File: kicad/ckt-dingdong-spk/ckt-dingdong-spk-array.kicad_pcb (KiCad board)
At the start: 2 copper layers, 96.5 x 96.5 mm, 224 parts, among them J1 Conn_01x02_MountingPin

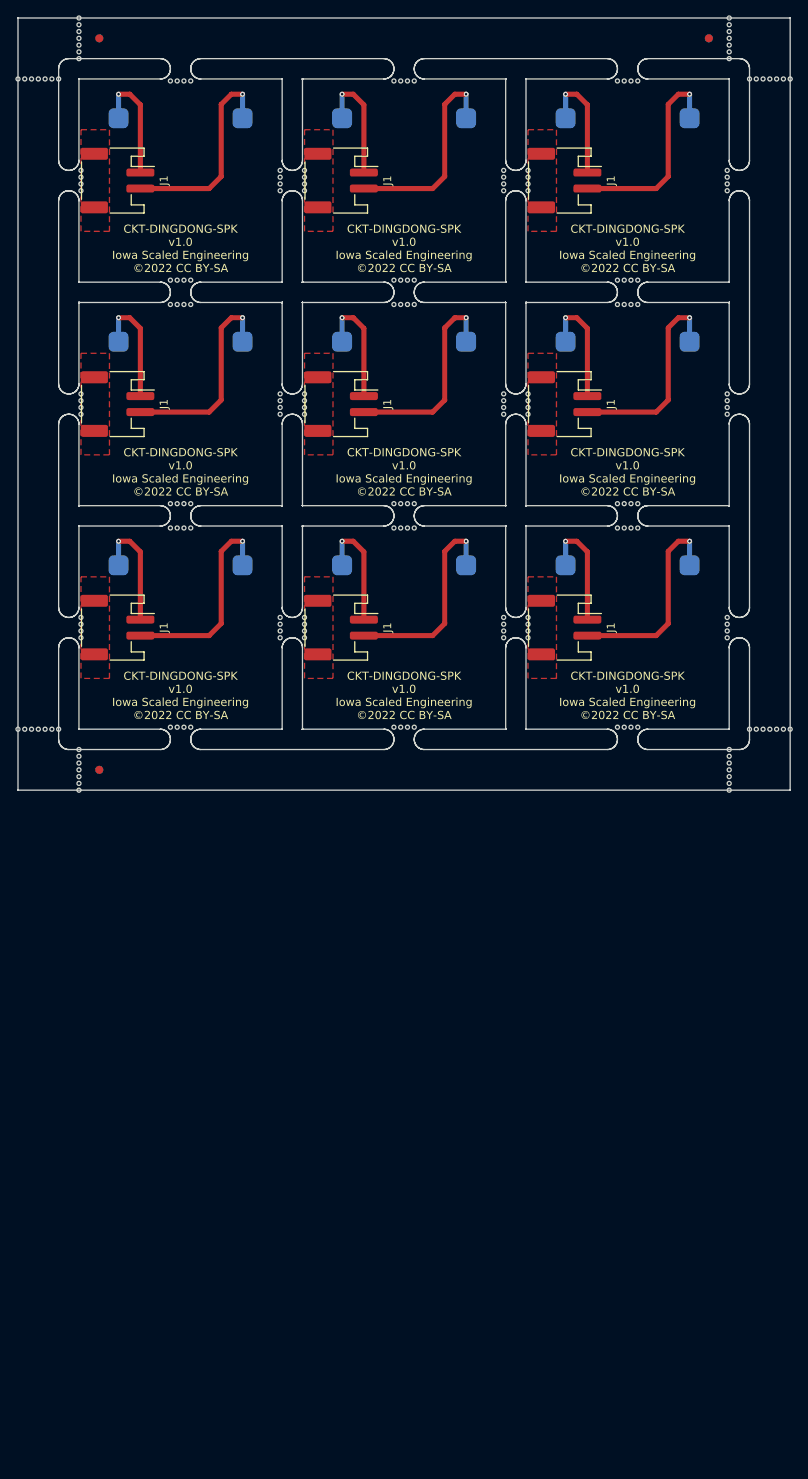
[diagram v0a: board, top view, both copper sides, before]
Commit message: Added array board
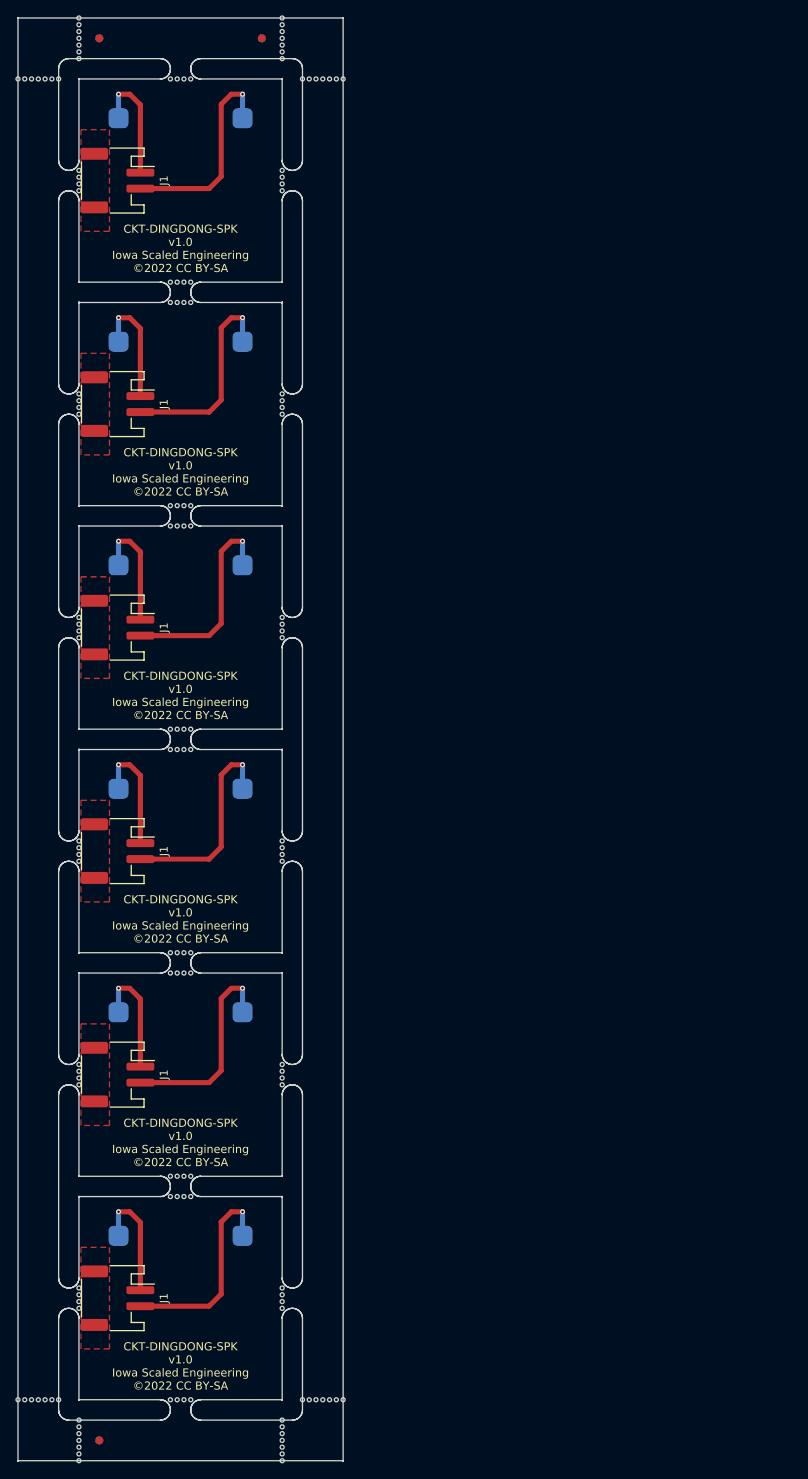
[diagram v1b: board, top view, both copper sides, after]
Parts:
- removed the J1 at (83.3, 91.2)
- removed the J1 at (55.4, 91.2)
- removed the J1 at (27.4, 91.2)
- removed the REF** at (19.2, 103.9)
- removed the REF** at (75.7, 63.7)
- removed the REF** at (36.6, 50.8)
- removed the REF** at (78.8, 64.5)
- removed the REF** at (92.5, 75.7)
- removed the REF** at (34.9, 103.7)
- removed the REF** at (34.9, 75.7)
- removed the REF** at (50.8, 64.5)
- removed the REF** at (78.8, 34.9)
- removed the REF** at (75.7, 34.0)
- removed the REF** at (47.8, 62.8)
- removed the REF** at (63.7, 75.7)
- removed the REF** at (78.8, 91.6)
- removed the REF** at (62.8, 47.8)
- removed the REF** at (90.8, 50.8)
- removed the REF** at (64.5, 50.8)
- removed the REF** at (22.9, 90.8)
- removed the REF** at (75.7, 36.6)
- removed the REF** at (103.9, 107.3)
- removed the REF** at (75.7, 34.9)
- removed the REF** at (106.4, 22.6)
- removed the REF** at (90.8, 103.7)
- removed the REF** at (103.7, 89.9)
- removed the REF** at (34.9, 78.8)
- removed the REF** at (50.8, 63.7)
- removed the REF** at (63.7, 78.8)
- removed the REF** at (34.0, 75.7)
- removed the REF** at (63.7, 50.8)
- removed the REF** at (47.8, 62.0)
- removed the REF** at (91.6, 50.8)
- removed the REF** at (17.5, 103.9)
- removed the REF** at (47.8, 89.9)
- removed the REF** at (103.9, 109.0)
- removed the REF** at (103.7, 34.9)
- removed the REF** at (50.8, 35.7)
- removed the REF** at (22.6, 107.3)
- removed the REF** at (62.8, 50.8)
- removed the REF** at (103.9, 110.7)
- removed the REF** at (50.8, 62.0)
- removed the REF** at (63.7, 103.7)
- removed the REF** at (92.5, 78.8)
- removed the REF** at (78.8, 62.0)
- removed the REF** at (75.7, 90.8)
- removed the REF** at (50.8, 92.5)
- removed the REF** at (50.8, 90.8)
- removed the REF** at (22.9, 35.7)
- removed the REF** at (62.0, 47.8)
- removed the REF** at (103.7, 36.6)
- removed the REF** at (103.9, 19.2)
- removed the REF** at (22.9, 62.8)
- removed the REF** at (108.1, 103.9)
- removed the REF** at (78.8, 35.7)
- removed the REF** at (106.4, 103.9)
- removed the REF** at (91.6, 22.9)
- removed the REF** at (78.8, 62.8)
- removed the REF** at (22.6, 111.5)
- removed the REF** at (103.9, 20.1)
- removed the REF** at (34.0, 78.8)
- removed the REF** at (89.9, 47.8)
- removed the REF** at (18.4, 103.9)
- removed the REF** at (91.6, 103.7)
- removed the REF** at (36.6, 47.8)
- removed the REF** at (36.6, 103.7)
- removed the REF** at (47.8, 91.6)
- removed the REF** at (64.5, 78.8)
- removed the REF** at (75.7, 35.7)
- removed the REF** at (50.8, 89.9)
- removed the REF** at (78.8, 92.5)
- removed the REF** at (34.9, 50.8)
- removed the REF** at (34.0, 47.8)
- removed the REF** at (110.7, 103.9)
- removed the REF** at (15.0, 103.9)
- removed the REF** at (90.8, 75.7)
- removed the REF** at (22.6, 110.7)
- removed the REF** at (101.4, 17.5) (x2)
- removed the REF** at (62.0, 22.9)
- removed the REF** at (108.1, 22.6)
- removed the REF** at (111.5, 22.6)
- removed the REF** at (103.9, 108.1)
- removed the REF** at (50.8, 34.9)
- removed the REF** at (35.7, 50.8)
- removed the REF** at (89.9, 103.7)
- removed the REF** at (89.9, 22.9)
- removed the REF** at (34.0, 103.7)
- removed the REF** at (63.7, 47.8)
- removed the REF** at (22.9, 64.5)
- removed the REF** at (47.8, 92.5)
- removed the REF** at (109.0, 22.6)
- removed the REF** at (62.8, 75.7)
- removed the REF** at (103.7, 34.0)
- removed the REF** at (103.7, 35.7)
- removed the REF** at (75.7, 62.0)
- removed the REF** at (22.6, 109.8)
- removed the REF** at (103.7, 62.0)
- removed the REF** at (15.8, 103.9)
- removed the REF** at (92.5, 22.9)
- removed the REF** at (47.8, 64.5)
- removed the REF** at (47.8, 90.8)
- removed the REF** at (22.9, 92.5)
- removed the REF** at (35.7, 47.8)
- removed the REF** at (78.8, 34.0)
- removed the REF** at (62.8, 78.8)
- removed the REF** at (75.7, 91.6)
- removed the REF** at (22.6, 109.0)
- removed the REF** at (78.8, 90.8)
- removed the REF** at (62.0, 50.8)
- removed the REF** at (35.7, 75.7)
- removed the REF** at (89.9, 50.8)
- removed the REF** at (25.2, 109.0) (x2)
- removed the REF** at (25.2, 17.5) (x2)
- removed the REF** at (75.7, 62.8)
- removed the REF** at (22.9, 62.0)
- removed the REF** at (78.8, 89.9)
- removed the REF** at (103.9, 16.7)
- removed the REF** at (35.7, 103.7)
- removed the REF** at (47.8, 34.0)
- removed the REF** at (63.7, 22.9)
- removed the REF** at (35.7, 22.9)
- removed the REF** at (62.8, 22.9)
- removed the REF** at (62.0, 103.7)
- removed the REF** at (22.9, 91.6)
- removed the REF** at (62.8, 103.7)
- removed the REF** at (109.8, 103.9)
- removed the REF** at (91.6, 47.8)
- removed the REF** at (103.7, 91.6)
- removed the REF** at (92.5, 47.8)
- removed the REF** at (103.9, 15.0)
- removed the REF** at (107.3, 22.6)
- removed the REF** at (34.9, 47.8)
- removed the REF** at (111.5, 103.9)
- removed the REF** at (64.5, 103.7)
- removed the REF** at (22.6, 108.1)
- removed the REF** at (78.8, 36.6)
- removed the REF** at (16.7, 103.9)
- removed the REF** at (92.5, 50.8)
- removed the REF** at (47.8, 36.6)
- removed the REF** at (22.9, 34.9)
- removed the REF** at (91.6, 75.7)
- removed the REF** at (103.9, 15.8)
- removed the REF** at (109.0, 103.9)
- removed the REF** at (47.8, 35.7)
- removed the REF** at (75.7, 92.5)
- removed the REF** at (36.6, 78.8)
- removed the REF** at (64.5, 47.8)
- removed the REF** at (75.7, 89.9)
- removed the REF** at (103.7, 90.8)
- removed the REF** at (22.6, 106.4)
- removed the REF** at (103.9, 111.5)
- removed the REF** at (90.8, 78.8)
- removed the REF** at (91.6, 78.8)
- removed the REF** at (110.7, 22.6)
- removed the REF** at (64.5, 22.9)
- removed the REF** at (22.9, 36.6)
- removed the REF** at (22.9, 63.7)
- removed the REF** at (36.6, 75.7)
- removed the REF** at (50.8, 62.8)
- removed the REF** at (75.7, 64.5)
- removed the REF** at (22.9, 34.0)
- removed the REF** at (62.0, 75.7)
- removed the REF** at (34.0, 22.9)
- removed the REF** at (20.1, 103.9)
- removed the REF** at (92.5, 103.7)
- removed the REF** at (50.8, 34.0)
- removed the REF** at (103.9, 18.4)
- removed the REF** at (103.7, 64.5)
- removed the REF** at (109.8, 22.6)
- removed the REF** at (103.7, 92.5)
- removed the REF** at (47.8, 63.7)
- removed the REF** at (36.6, 22.9)
- removed the REF** at (50.8, 36.6)
- removed the REF** at (22.9, 89.9)
- removed the REF** at (103.9, 106.4)
- removed the REF** at (90.8, 47.8)
- removed the REF** at (89.9, 78.8)
- removed the REF** at (90.8, 22.9)
- removed the REF** at (35.7, 78.8)
- removed the REF** at (103.7, 62.8)
- removed the REF** at (50.8, 91.6)
- removed the REF** at (103.9, 17.5)
- removed the REF** at (103.7, 63.7)
- removed the REF** at (107.3, 103.9)
- removed the REF** at (89.9, 75.7)
- removed the REF** at (103.9, 109.8)
- removed the REF** at (62.0, 78.8)
- removed the REF** at (34.9, 22.9)
- removed the REF** at (64.5, 75.7)
- removed the REF** at (78.8, 63.7)
- removed the REF** at (47.8, 34.9)
- removed the REF** at (34.0, 50.8)
- removed the SPK1 at (35.3, 88.7)
- removed the SPK1 at (63.3, 88.7)
- removed the SPK1 at (91.2, 88.7)
- added REF**: NPTH, NPTH, F.Cu at (53.9, 187.7)
- added REF**: NPTH, NPTH, F.Cu at (34.9, 134.4)
- added REF**: Fiducial, Fiducial, F.Cu at (45.5, 17.5)
- added REF**: NPTH, NPTH, F.Cu at (34.9, 76.0)
- added REF**: NPTH, NPTH, F.Cu at (34.9, 48.0)
- added REF**: NPTH, NPTH, F.Cu at (36.6, 48.0)
- added REF**: NPTH, NPTH, F.Cu at (52.3, 22.6)
- added REF**: NPTH, NPTH, F.Cu at (22.6, 194.5)
- added REF**: NPTH, NPTH, F.Cu at (22.6, 118.7)
- added REF**: NPTH, NPTH, F.Cu at (35.7, 187.7)
- added REF**: NPTH, NPTH, F.Cu at (48.0, 191.1)
- added REF**: NPTH, NPTH, F.Cu at (22.6, 147.5)
- added REF**: NPTH, NPTH, F.Cu at (55.6, 187.7)
- added REF**: NPTH, NPTH, F.Cu at (48.0, 194.5)
- added REF**: NPTH, NPTH, F.Cu at (36.6, 162.3)
- added REF**: NPTH, NPTH, F.Cu at (36.6, 22.6)
- added REF**: NPTH, NPTH, F.Cu at (34.9, 106.4)
- added REF**: NPTH, NPTH, F.Cu at (48.0, 120.4)
- added REF**: NPTH, NPTH, F.Cu at (48.0, 18.4)
- added REF**: NPTH, NPTH, F.Cu at (34.0, 134.4)
- added REF**: NPTH, NPTH, F.Cu at (22.6, 36.6)
- added REF**: NPTH, NPTH, F.Cu at (22.6, 92.5)
- added REF**: NPTH, NPTH, F.Cu at (17.5, 187.7)
- added REF**: NPTH, NPTH, F.Cu at (48.0, 192.0)
- added REF**: NPTH, NPTH, F.Cu at (22.6, 34.0)
- added REF**: NPTH, NPTH, F.Cu at (53.9, 22.6)
- added REF**: NPTH, NPTH, F.Cu at (19.2, 187.7)
- added REF**: NPTH, NPTH, F.Cu at (34.0, 159.8)
- added REF**: NPTH, NPTH, F.Cu at (36.6, 50.6)
- added REF**: NPTH, NPTH, F.Cu at (22.6, 174.6)
- added REF**: NPTH, NPTH, F.Cu at (48.0, 90.8)
- added REF**: NPTH, NPTH, F.Cu at (22.6, 191.1)
- added REF**: NPTH, NPTH, F.Cu at (34.9, 159.8)
- added REF**: NPTH, NPTH, F.Cu at (15.0, 187.7)
- added REF**: NPTH, NPTH, F.Cu at (22.6, 146.7)
- added REF**: NPTH, NPTH, F.Cu at (34.9, 187.7)
- added REF**: NPTH, NPTH, F.Cu at (22.6, 62.0)
- added REF**: NPTH, NPTH, F.Cu at (34.9, 131.8)
- added REF**: NPTH, NPTH, F.Cu at (48.0, 92.5)
- added REF**: NPTH, NPTH, F.Cu at (22.6, 34.9)
- added REF**: NPTH, NPTH, F.Cu at (36.6, 78.5)
- added REF**: NPTH, NPTH, F.Cu at (35.7, 22.6)
- added REF**: NPTH, NPTH, F.Cu at (22.6, 119.6)
- added REF**: NPTH, NPTH, F.Cu at (22.6, 175.4)
- added REF**: NPTH, NPTH, F.Cu at (48.0, 15.0)
- added REF**: NPTH, NPTH, F.Cu at (35.7, 50.6)
- added REF**: NPTH, NPTH, F.Cu at (50.6, 22.6)
- added REF**: NPTH, NPTH, F.Cu at (48.0, 190.3)
- added REF**: NPTH, NPTH, F.Cu at (35.7, 78.5)
- added REF**: NPTH, NPTH, F.Cu at (34.0, 106.4)
- added REF**: NPTH, NPTH, F.Cu at (51.4, 187.7)
- added REF**: NPTH, NPTH, F.Cu at (48.0, 176.3)
- added REF**: NPTH, NPTH, F.Cu at (22.6, 176.3)
- added REF**: NPTH, NPTH, F.Cu at (34.9, 50.6)
- added REF**: NPTH, NPTH, F.Cu at (34.0, 50.6)
- added REF**: NPTH, NPTH, F.Cu at (22.6, 35.7)
- added REF**: NPTH, NPTH, F.Cu at (36.6, 159.8)
- added REF**: Fiducial, Fiducial, B.Cu at (25.2, 192.8)
- added REF**: Fiducial, Fiducial, B.Cu at (45.5, 17.5)
- added REF**: Fiducial, Fiducial, B.Cu at (25.2, 17.5)
- added REF**: NPTH, NPTH, F.Cu at (36.6, 106.4)
- added REF**: NPTH, NPTH, F.Cu at (34.9, 78.5)
- added REF**: NPTH, NPTH, F.Cu at (35.7, 131.8)
- added REF**: NPTH, NPTH, F.Cu at (48.0, 35.7)
- added REF**: NPTH, NPTH, F.Cu at (35.7, 48.0)
- added REF**: NPTH, NPTH, F.Cu at (35.7, 162.3)
- added REF**: NPTH, NPTH, F.Cu at (48.0, 20.1)
- added REF**: NPTH, NPTH, F.Cu at (48.0, 147.5)
- added REF**: NPTH, NPTH, F.Cu at (22.6, 120.4)
- added REF**: NPTH, NPTH, F.Cu at (34.0, 78.5)
- added REF**: NPTH, NPTH, F.Cu at (22.6, 195.3)
- added REF**: NPTH, NPTH, F.Cu at (52.3, 187.7)
- added REF**: NPTH, NPTH, F.Cu at (36.6, 76.0)
- added REF**: NPTH, NPTH, F.Cu at (22.6, 193.6)
- added REF**: NPTH, NPTH, F.Cu at (15.8, 187.7)
- added REF**: NPTH, NPTH, F.Cu at (48.0, 17.5)
- added REF**: NPTH, NPTH, F.Cu at (48.0, 118.7)
- added REF**: NPTH, NPTH, F.Cu at (54.8, 187.7)
- added REF**: NPTH, NPTH, F.Cu at (16.7, 187.7)
- added REF**: NPTH, NPTH, F.Cu at (48.0, 62.8)
- added REF**: NPTH, NPTH, F.Cu at (48.0, 64.5)
- added REF**: NPTH, NPTH, F.Cu at (20.1, 187.7)
- added REF**: NPTH, NPTH, F.Cu at (53.1, 22.6)
- added REF**: NPTH, NPTH, F.Cu at (22.6, 64.5)
- added REF**: NPTH, NPTH, F.Cu at (48.0, 36.6)
- added REF**: NPTH, NPTH, F.Cu at (36.6, 131.8)
- added REF**: NPTH, NPTH, F.Cu at (48.0, 173.8)
- added REF**: NPTH, NPTH, F.Cu at (36.6, 187.7)
- added REF**: NPTH, NPTH, F.Cu at (35.7, 106.4)
- added REF**: NPTH, NPTH, F.Cu at (22.6, 63.7)
- added REF**: NPTH, NPTH, F.Cu at (36.6, 103.9)
- added REF**: NPTH, NPTH, F.Cu at (35.7, 159.8)
- added REF**: Fiducial, Fiducial, F.Cu at (25.2, 17.5)
- added REF**: NPTH, NPTH, F.Cu at (22.6, 192.0)
- added REF**: NPTH, NPTH, F.Cu at (48.0, 148.3)
- added REF**: NPTH, NPTH, F.Cu at (22.6, 91.6)
- added REF**: NPTH, NPTH, F.Cu at (22.6, 62.8)
- added REF**: NPTH, NPTH, F.Cu at (54.8, 22.6)
- added REF**: NPTH, NPTH, F.Cu at (48.0, 62.0)
- added REF**: NPTH, NPTH, F.Cu at (34.0, 22.6)
- added REF**: NPTH, NPTH, F.Cu at (48.0, 16.7)
- added REF**: NPTH, NPTH, F.Cu at (34.0, 162.3)
- added REF**: NPTH, NPTH, F.Cu at (48.0, 34.0)
- added REF**: NPTH, NPTH, F.Cu at (34.0, 103.9)
- added REF**: NPTH, NPTH, F.Cu at (36.6, 134.4)
- added REF**: NPTH, NPTH, F.Cu at (48.0, 34.9)
- added REF**: NPTH, NPTH, F.Cu at (48.0, 89.9)
- added REF**: NPTH, NPTH, F.Cu at (35.7, 134.4)
- added REF**: NPTH, NPTH, F.Cu at (48.0, 19.2)
- added REF**: NPTH, NPTH, F.Cu at (34.0, 76.0)
- added REF**: NPTH, NPTH, F.Cu at (18.4, 187.7)
- added REF**: NPTH, NPTH, F.Cu at (34.0, 187.7)
- added REF**: NPTH, NPTH, F.Cu at (22.6, 145.8)
- added REF**: NPTH, NPTH, F.Cu at (50.6, 187.7)
- added REF**: NPTH, NPTH, F.Cu at (35.7, 103.9)
- added REF**: NPTH, NPTH, F.Cu at (48.0, 193.6)
- added REF**: NPTH, NPTH, F.Cu at (34.0, 48.0)
- added REF**: NPTH, NPTH, F.Cu at (48.0, 174.6)
- added REF**: NPTH, NPTH, F.Cu at (34.0, 131.8)
- added REF**: NPTH, NPTH, F.Cu at (35.7, 76.0)
- added REF**: NPTH, NPTH, F.Cu at (48.0, 119.6)
- added REF**: NPTH, NPTH, F.Cu at (22.6, 89.9)
- added REF**: NPTH, NPTH, F.Cu at (22.6, 192.8)
- added REF**: NPTH, NPTH, F.Cu at (48.0, 195.3)
- added REF**: NPTH, NPTH, F.Cu at (34.9, 22.6)
- added REF**: NPTH, NPTH, F.Cu at (48.0, 145.8)
- added REF**: NPTH, NPTH, F.Cu at (48.0, 63.7)
- added REF**: NPTH, NPTH, F.Cu at (48.0, 15.8)
- added REF**: NPTH, NPTH, F.Cu at (22.6, 117.9)
- added REF**: NPTH, NPTH, F.Cu at (22.6, 173.8)
- added REF**: NPTH, NPTH, F.Cu at (53.1, 187.7)
- added REF**: NPTH, NPTH, F.Cu at (48.0, 91.6)
- added REF**: NPTH, NPTH, F.Cu at (34.9, 103.9)
- added REF**: NPTH, NPTH, F.Cu at (34.9, 162.3)
- added REF**: NPTH, NPTH, F.Cu at (22.6, 148.3)
- added REF**: NPTH, NPTH, F.Cu at (48.0, 175.4)
- added REF**: NPTH, NPTH, F.Cu at (51.4, 22.6)
- added REF**: NPTH, NPTH, F.Cu at (48.0, 146.7)
- added REF**: NPTH, NPTH, F.Cu at (22.6, 190.3)
- added REF**: NPTH, NPTH, F.Cu at (55.6, 22.6)
- added REF**: NPTH, NPTH, F.Cu at (48.0, 117.9)
- added REF**: Fiducial, Fiducial, F.Cu at (25.2, 192.8)
- added REF**: NPTH, NPTH, F.Cu at (48.0, 192.8)
- added REF**: NPTH, NPTH, F.Cu at (22.6, 90.8)
- moved J1 125.0 mm to (27.4, 175.0)
- moved SPK1 125.0 mm to (35.3, 172.5)
- moved J1 88.4 mm to (27.4, 147.1)
- moved SPK1 88.4 mm to (35.3, 144.5)
- moved J1 79.0 mm to (27.4, 91.2)
- moved SPK1 79.0 mm to (35.3, 88.7)
- moved J1 55.9 mm to (27.4, 119.1)
- moved SPK1 55.9 mm to (35.3, 116.6)
- moved J1 39.5 mm to (27.4, 63.3)
- moved SPK1 39.5 mm to (35.3, 60.7)
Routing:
- net Board_8-Net-(SPK1-Pad1): track 25.9 -> 0.00 mm, vias 1 -> 0
- net Board_6-Net-(SPK1-Pad1): track 25.9 -> 0.00 mm, vias 1 -> 0
- net Board_7-Net-(SPK1-Pad1): track 25.9 -> 0.00 mm, vias 1 -> 0
- net Board_7-Net-(SPK1-Pad2): track 14.7 -> 0.00 mm, vias 1 -> 0
- net Board_6-Net-(SPK1-Pad2): track 14.7 -> 0.00 mm, vias 1 -> 0
- net Board_8-Net-(SPK1-Pad2): track 14.7 -> 0.00 mm, vias 1 -> 0
- removed copper zone on F.Cu, net Board_6-/MP
- removed copper zone on F.Cu, net Board_7-/MP
- removed copper zone on F.Cu, net Board_8-/MP
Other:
- board size 96.5 x 96.5 mm -> 40.6 x 180.3 mm
